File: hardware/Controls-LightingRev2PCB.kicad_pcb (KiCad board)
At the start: 2 copper layers, 52 parts, among them IC1 LM74502HDDFR, IC2 TLV70433DBVT, J2 759001181, J3 53307-2471, J4 Conn_02x08_Top_Bottom, Q1 PSMN8R5-40MSDX, Q2 IRLML0030, Q3 IRLML0030, U1 TLV2371DBV, U2 INA241A5xD, U3 INA241A5xD, U4 INA241A5xD, U5 SN74LV1T34DBV, U8 TLV2371DBV, U9 TLV2371DBV

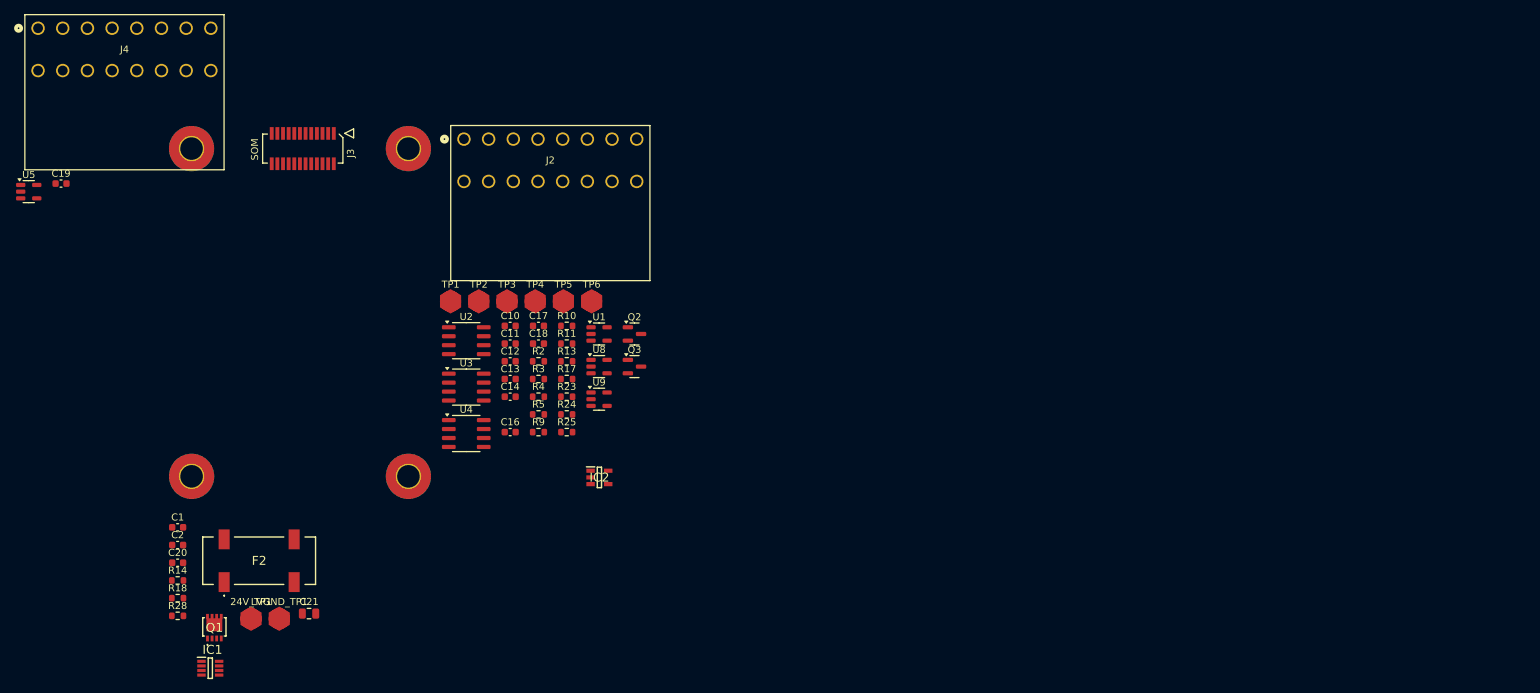
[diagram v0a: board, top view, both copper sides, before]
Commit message: New board dimensions
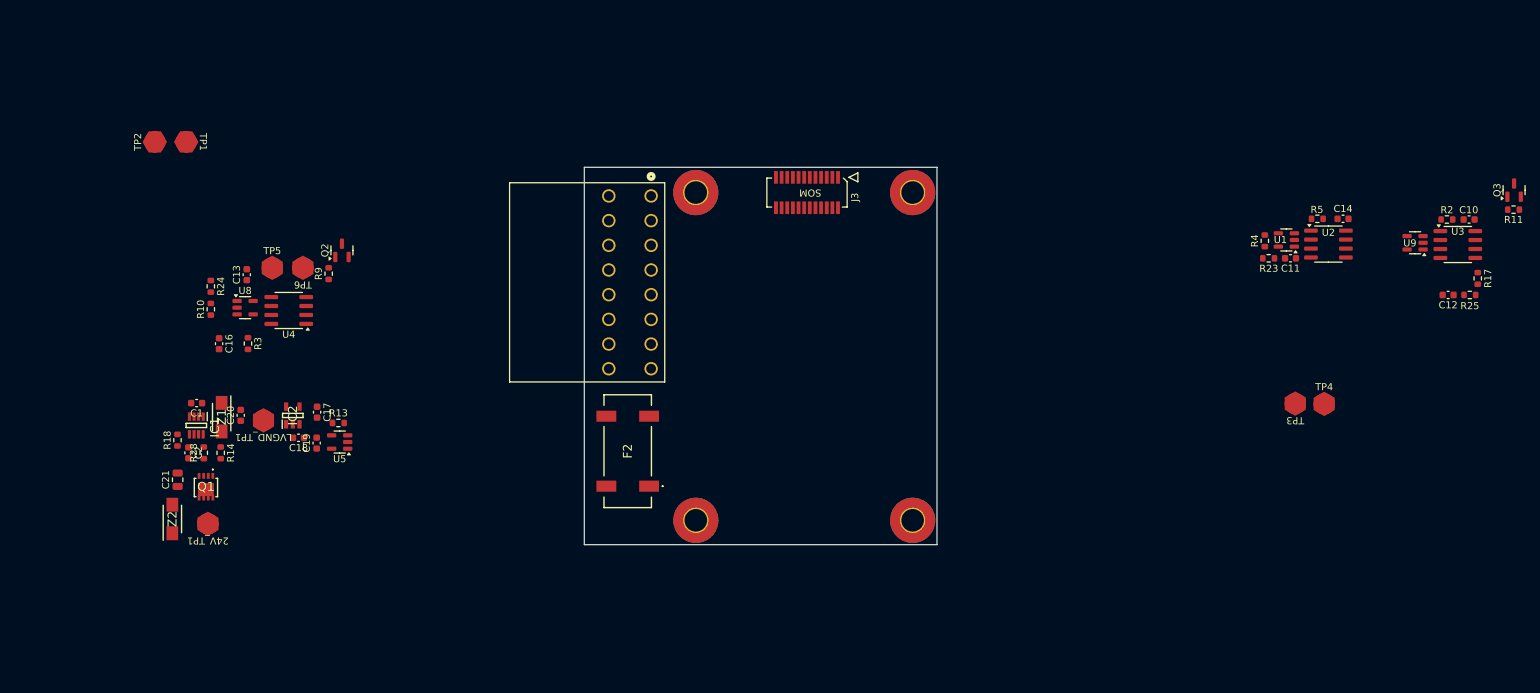
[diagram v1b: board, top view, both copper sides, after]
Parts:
- removed J2: 759001181, MX150:CONN_SD-75900-001_2X08_MOL
- added Z1: SMAF4751A-TP, UTSVT_Passive:SODFL5026X125N, F.Cu at (29.4, 57.3)
- added Z2: SMAF4751A-TP, UTSVT_Passive:SODFL5026X125N, F.Cu at (22.4, 71.7)
- R13: value 1k -> 100
- moved U3 142.0 mm to (204.7, 32.8)
- moved C10 136.8 mm to (206.3, 29.2)
- moved R11 135.6 mm to (212.6, 27.9), turned to 180 degrees
- moved C12 133.3 mm to (203.3, 40.0), turned to 180 degrees
- moved R2 130.4 mm to (203.2, 29.2), turned to 180 degrees
- moved R17 130.0 mm to (207.5, 37.6), turned to 90 degrees
- moved R25 129.5 mm to (206.4, 40.0)
- moved Q3 127.2 mm to (212.7, 25.1), turned to 90 degrees
- moved U2 123.0 mm to (186.3, 32.7)
- moved C14 120.8 mm to (188.4, 29.1)
- moved U9 117.8 mm to (198.6, 32.5), turned to 180 degrees
- moved R5 113.9 mm to (184.8, 29.1), turned to 180 degrees
- moved TP4 112.8 mm to (185.8, 55.4)
- moved TP3 112.7 mm to (181.7, 55.4), turned to 180 degrees
- moved C11 111.3 mm to (181.0, 34.8), turned to 180 degrees
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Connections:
- C10 pad 1: +24V -> Addressable_GND
- C10 pad 2: Addressable_GND -> +24V
- C11 pad 1: +3.3V -> Addressable_GND
- C11 pad 2: Addressable_GND -> +3.3V
- C13 pad 1: +3.3V -> Addressable_GND
- C13 pad 2: Addressable_GND -> +3.3V
- C14 pad 1: +24V -> Addressable_GND
- C14 pad 2: Addressable_GND -> +24V
- C16 pad 1: +24V -> Addressable_GND
- C16 pad 2: Addressable_GND -> +24V
- C17 pad 1: 5V PWR -> Addressable_GND
- C17 pad 2: Addressable_GND -> 5V PWR
- C18 pad 1: +24V -> Addressable_GND
- C18 pad 2: Addressable_GND -> +24V
- C19 pad 1: 5V PWR -> Addressable_GND
- C19 pad 2: Addressable_GND -> 5V PWR
- J4 pad 1: +24V -> 24V_Ext
- J4 pad 10: Strobe_GND -> CAN_H
- J4 pad 11: Strobe_PWR -> CAN_L
- J4 pad 12: Normal_GND -> Addressable_GND
- J4 pad 13: Normal_PWR -> Addressable_GND
- J4 pad 15: unconnected-(J4-Pin_15-Pad15) -> Strobe_GND
- J4 pad 16: Addressable_GND -> Normal_GND
- J4 pad 2: 24V_Ext -> CAN_H
- J4 pad 3: CAN_H -> CAN_L
- J4 pad 4: CAN_L -> Addressable_GND
- J4 pad 5: CAN_H -> Addressable_PWR
- J4 pad 6: CAN_L -> Addressable_Logic
- J4 pad 7: Addressable_GND -> Strobe_PWR
- J4 pad 8: Addressable_Logic -> Normal_PWR
- J4 pad 9: Addressable_PWR -> 24V_Ext
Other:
- board outline added: 50 x 53.5 mm

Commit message: Componenent Layout, I branched into MX150_Connectors however, I can't seem to find the 2x8 connector. It's probably an issue on my end but I can look into it later
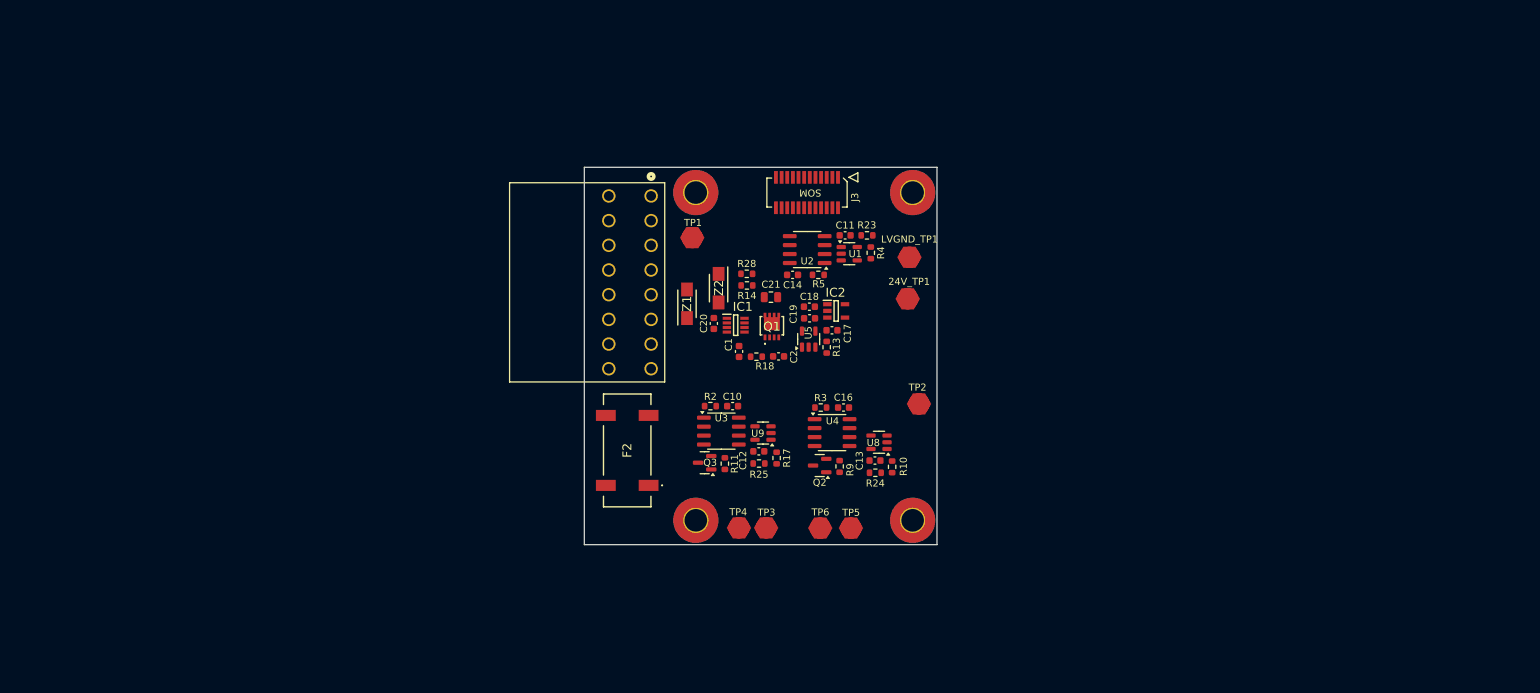
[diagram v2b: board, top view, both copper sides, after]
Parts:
- moved Q3 121.1 mm to (97.9, 63.7), turned to 180 degrees
- moved R11 117.5 mm to (100.8, 63.9), turned to -90 degrees
- moved TP2 114.5 mm to (128.3, 55.4)
- moved C10 107.7 mm to (101.9, 55.7)
- moved R2 107.7 mm to (98.7, 55.7)
- moved U3 107.7 mm to (100.3, 59.3)
- moved 24V_TP1 104.2 mm to (126.7, 40.5), turned to 90 degrees
- moved R25 103.6 mm to (105.6, 63.8)
- moved R17 102.6 mm to (108.1, 63.1)
- moved C12 100.2 mm to (105.6, 62.1)
- moved R10 99.2 mm to (124.5, 64.3)
- moved R24 97.9 mm to (122.1, 65.2), turned to 0 degrees
- moved U9 96.3 mm to (106.2, 59.5)
- moved LVGND_TP1 94.5 mm to (127.0, 34.6), turned to 90 degrees
- moved C13 92.9 mm to (122.1, 63.4), turned to 180 degrees
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
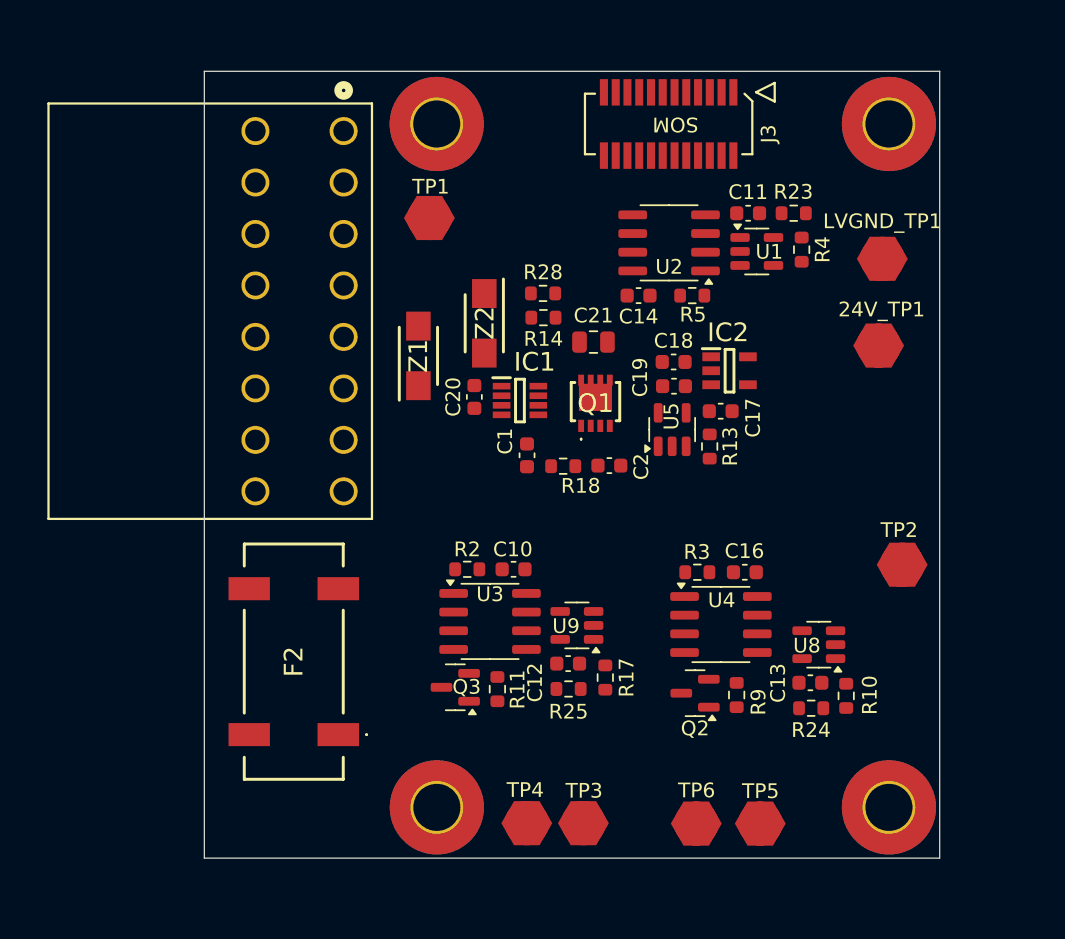
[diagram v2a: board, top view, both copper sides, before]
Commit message: Routed but having issues with gnd being pretty isolated
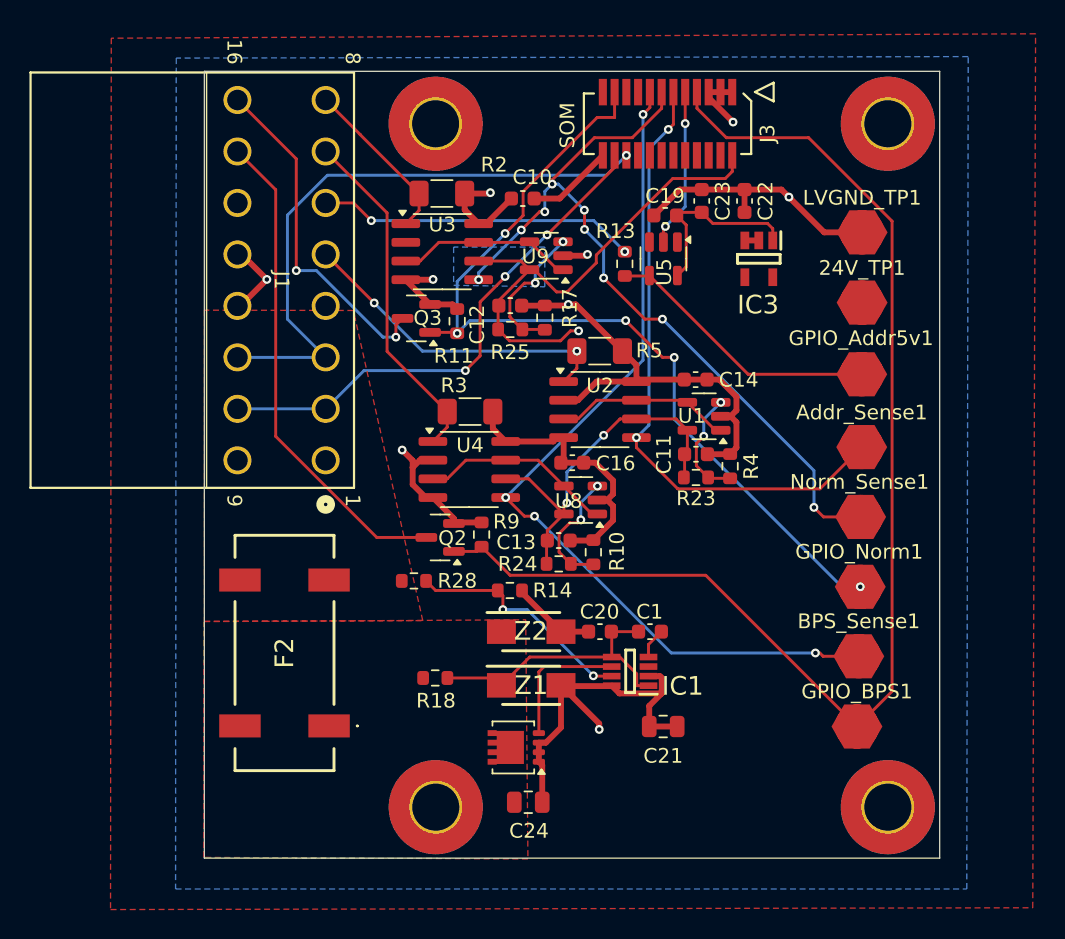
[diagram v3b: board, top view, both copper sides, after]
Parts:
- removed C17: 1uF, Capacitor_SMD:C_0603_1608Metric
- removed C18: 0.1uF, Capacitor_SMD:C_0603_1608Metric
- removed C2: 22n, Capacitor_SMD:C_0603_1608Metric
- removed IC2: TLV70433DBVT, MX_Connector:SOT95P280X145-5N
- removed J4: Conn_02x08_Top_Bottom, MX150:CONN_SD-75900-001_2X08_MOL
- removed Q1: PSMN8R5-40MSDX, UTSVT_Power:PSMN8R5-40MSDX
- removed TP1, TP2, TP3, TP4, TP5, TP6: TestPoint, UTSVT_Special:TestPoint_HEX_3mmID
- added Addr_Sense1: TestPoint, UTSVT_Special:TestPoint_HEX_3mmID, F.Cu at (125.5, 47.4)
- added BPS_Sense1: TestPoint, UTSVT_Special:TestPoint_HEX_3mmID, F.Cu at (125.3, 61.6)
- added C22: 0.1uF, Capacitor_SMD:C_0603_1608Metric, F.Cu at (117.6, 30.7)
- added C23: 1uF, Capacitor_SMD:C_0603_1608Metric, F.Cu at (114.7, 30.7)
- added C24: 220u, Capacitor_SMD:C_0805_2012Metric, F.Cu at (102.9, 71.5)
- added GPIO_Addr5v1: TestPoint, UTSVT_Special:TestPoint_HEX_3mmID, F.Cu at (125.5, 42.5)
- added GPIO_BPS1: TestPoint, UTSVT_Special:TestPoint_HEX_3mmID, F.Cu at (125.2, 66.4)
- added GPIO_Norm1: TestPoint, UTSVT_Special:TestPoint_HEX_3mmID, F.Cu at (125.5, 56.9)
- added IC3: TLV70130DBVR, UTSVT_Power:TLV70130DBVR, F.Cu at (118.5, 34.6)
- added J1: MX150_02x08_RightAngle, UTSVT_Connectors:CONN_SD-75900-001_2X08_MOL, F.Cu at (86.1, 36.1)
- added Norm_Sense1: TestPoint, UTSVT_Special:TestPoint_HEX_3mmID, F.Cu at (125.5, 52.1)
- added Q4: PSMN8R5-40MSDX, UTSVT_Power:PSMN8R5-40MSDX, F.Cu at (102.0, 67.9)
- C21: value 10u -> 220u
- R2, R3, R5: footprint Resistor_SMD:R_0603_1608Metric -> Resistor_SMD:R_1206_3216Metric_Pad1.30x1.75mm_HandSolder
- moved C21 26.6 mm to (112.0, 66.4)
- moved R2 25.6 mm to (97.0, 30.2)
- moved U3 25.3 mm to (97.0, 34.1)
- moved U9 25.2 mm to (104.1, 34.4)
- moved Q3 25.2 mm to (95.3, 38.6)
- moved C10 25.2 mm to (102.5, 30.5), turned to 180 degrees
- moved R11 25.2 mm to (98.0, 38.8)
- moved R17 24.8 mm to (104.0, 38.6)
- moved R25 24.8 mm to (101.7, 39.4)
- moved C12 24.7 mm to (101.7, 37.8)
- moved Z1 23.7 mm to (103.1, 63.6), turned to 0 degrees
- moved R28 21.4 mm to (95.1, 56.5)
- moved Z2 21.2 mm to (103.1, 60.0), turned to 0 degrees
- moved R9 20.5 mm to (99.7, 53.4)
- moved Q2 20.3 mm to (96.9, 53.5)
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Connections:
- C10 pad 1: Addressable_GND -> +24V
- C11 pad 1: Addressable_GND -> +24V
- C12 pad 1: Addressable_GND -> +24V
- C13 pad 1: Addressable_GND -> +24V
- C14 pad 1: Addressable_GND -> +24V
- C16 pad 1: Addressable_GND -> +24V
- C19 pad 1: Addressable_GND -> +24V
- C20 pad 1: Addressable_GND -> +24V
- C21 pad 2: Addressable_GND -> +24V
- F2 pad 1: Net-(Q1-S_1) -> Net-(Q4-D)
- IC1 pad 2: Addressable_GND -> +24V
- J3 pad 1: Addressable_GND -> +24V
- J3 pad 3: Addressable_GND -> +24V
- J3 pad 5: Addressable_GND -> +24V
- LVGND_TP1 pad 1: Addressable_GND -> +24V
- Q2 pad 2: Addressable_GND -> +24V
- Q3 pad 2: Addressable_GND -> +24V
- R10 pad 2: Addressable_GND -> +24V
- R11 pad 1: Addressable_GND -> +24V
- R14 pad 2: Addressable_GND -> +24V
- R17 pad 2: Addressable_GND -> +24V
- R18 pad 1: Net-(Q1-S_1) -> Net-(Q4-D)
- R4 pad 2: Addressable_GND -> +24V
- R9 pad 1: Addressable_GND -> +24V
- U1 pad 2: Addressable_GND -> +24V
- U2 pad 2: Addressable_GND -> +24V
- U2 pad 4: Addressable_GND -> +24V
- U3 pad 4: Addressable_GND -> +24V
- U4 pad 2: Addressable_GND -> +24V
- U4 pad 4: Addressable_GND -> +24V
- U8 pad 2: Addressable_GND -> +24V
- U9 pad 2: Addressable_GND -> +24V
- Z1 pad 2: Addressable_GND -> +24V
- Z2 pad 1: 24V_Ext -> Net-(Q4-D)
- Z2 pad 2: Addressable_GND -> +24V
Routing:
- net +24V: track 0.00 -> 141.5 mm, vias 0 -> 9
- net GPIO_BPS_Strobe: track 0.00 -> 85.5 mm
- net GPIO_Normal: track 0.00 -> 61.1 mm, vias 0 -> 5
- net BPS_Sense: track 0.00 -> 60.1 mm, vias 0 -> 4
- net +3.3V: track 0.00 -> 59.0 mm, vias 0 -> 3
- net NORMAL_Sense: track 0.00 -> 53.4 mm, vias 0 -> 9
- net ADDR_Sense: track 0.00 -> 42.9 mm, vias 0 -> 2
- net CAN_L: track 0.00 -> 41.5 mm, vias 0 -> 1
- net CAN_H: track 0.00 -> 35.4 mm, vias 0 -> 3
- net Strobe_GND: track 0.00 -> 33.5 mm
- net Strobe_PWR: track 0.00 -> 23.5 mm
- net Normal_GND: track 0.00 -> 23.4 mm, vias 0 -> 2
- net Addressable_PWR: track 0.00 -> 22.2 mm, vias 0 -> 2
- net Addressable_Logic: track 0.00 -> 21.7 mm, vias 0 -> 2
- net /Reverse Polarity Protection/RPP_EN: track 0.00 -> 19.5 mm
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- added copper zone on B.Cu, net +24V
- added copper zone on B.Cu, net +3.3V
- added copper zone on F.Cu, net 24V_Ext
- added copper zone on F.Cu, net Addressable_GND
- added copper zone on F.Cu, net Net-(Q4-D)
